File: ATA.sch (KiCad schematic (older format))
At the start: 12 parts, among them J1 TCOUPLE_IN, J2 Conn_01x08_Male, U1 AD8495, U2 AD8605

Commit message: updates
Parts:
- U2: symbol dk_Linear-Amplifiers-Instrumentation-OP-Amps-Buffer-Amps:AD8605ARTZ-REEL7 -> ATA-rescue:AD8605ARTZ-REEL7-dk_Linear-Amplifiers-Instrumentation-OP-Amps-Buffer-Amps
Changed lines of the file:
@@
 	5800 3400 5900 3400
 $Comp
-L dk_Linear-Amplifiers-Instrumentation-OP-Amps-Buffer-Amps:AD8605ARTZ-REEL7 U2
+L ATA-rescue:AD8605ARTZ-REEL7-dk_Linear-Amplifiers-Instrumentation-OP-Amps-Buffer-Amps U2
 U 1 1 5DF80621
 P 6700 4750

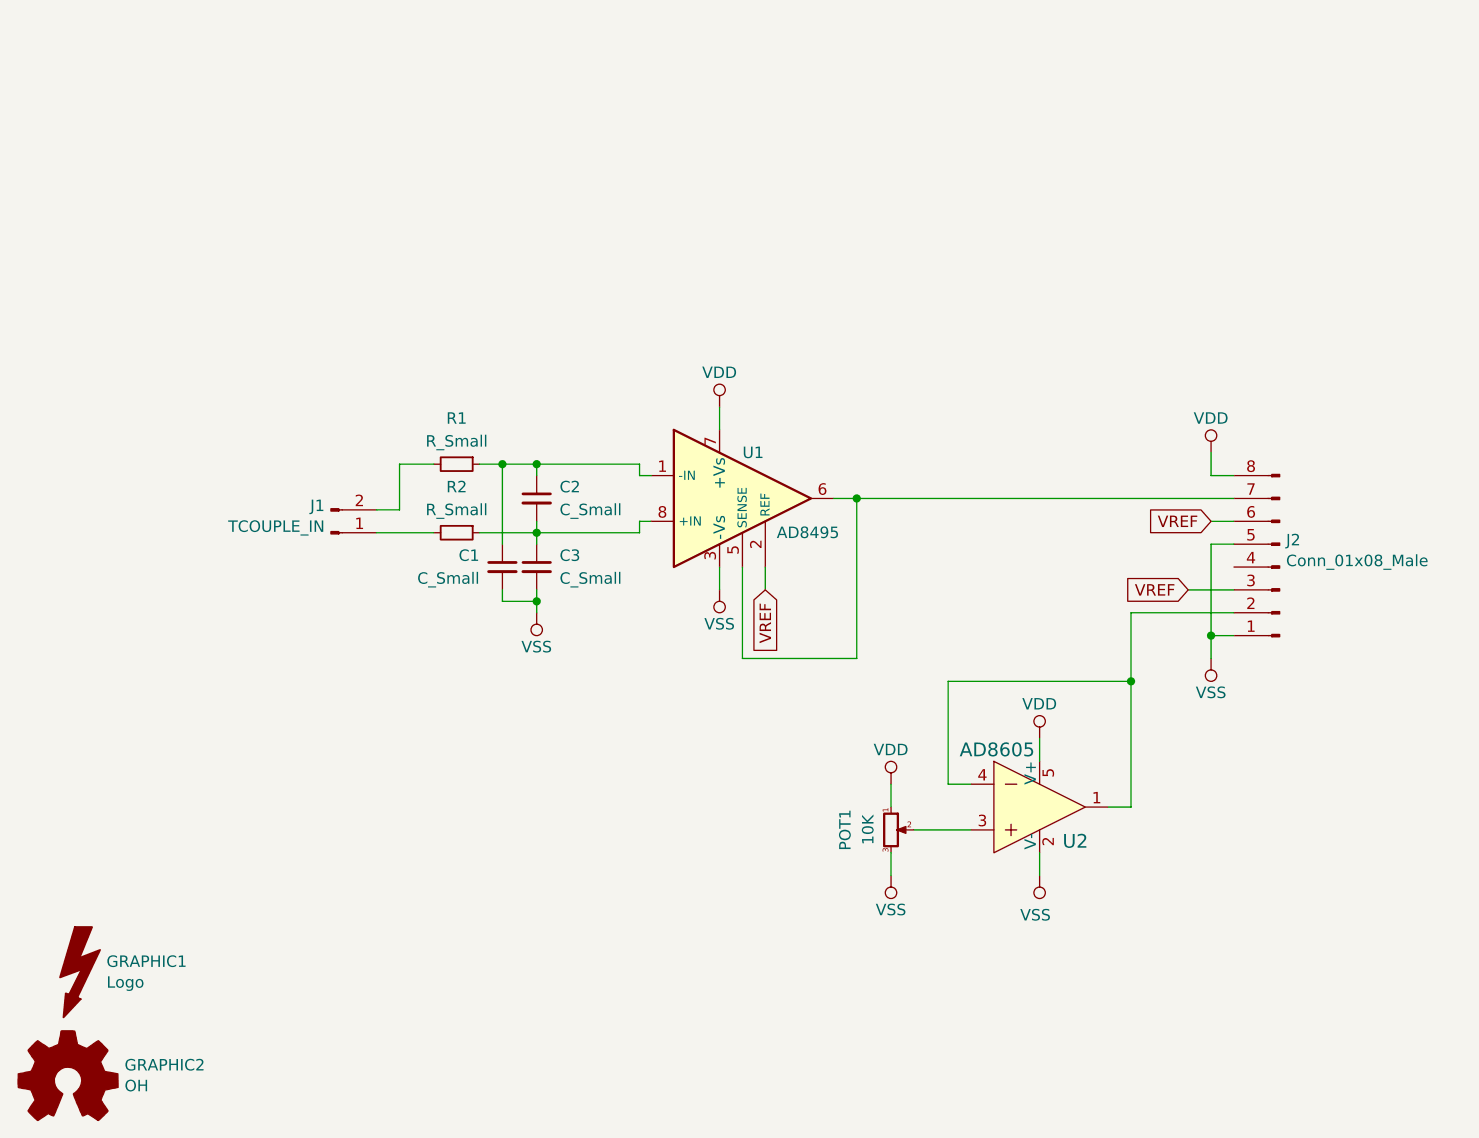
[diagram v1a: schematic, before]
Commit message: Added voltage reference chip to high side of adjustable voltage divider reference
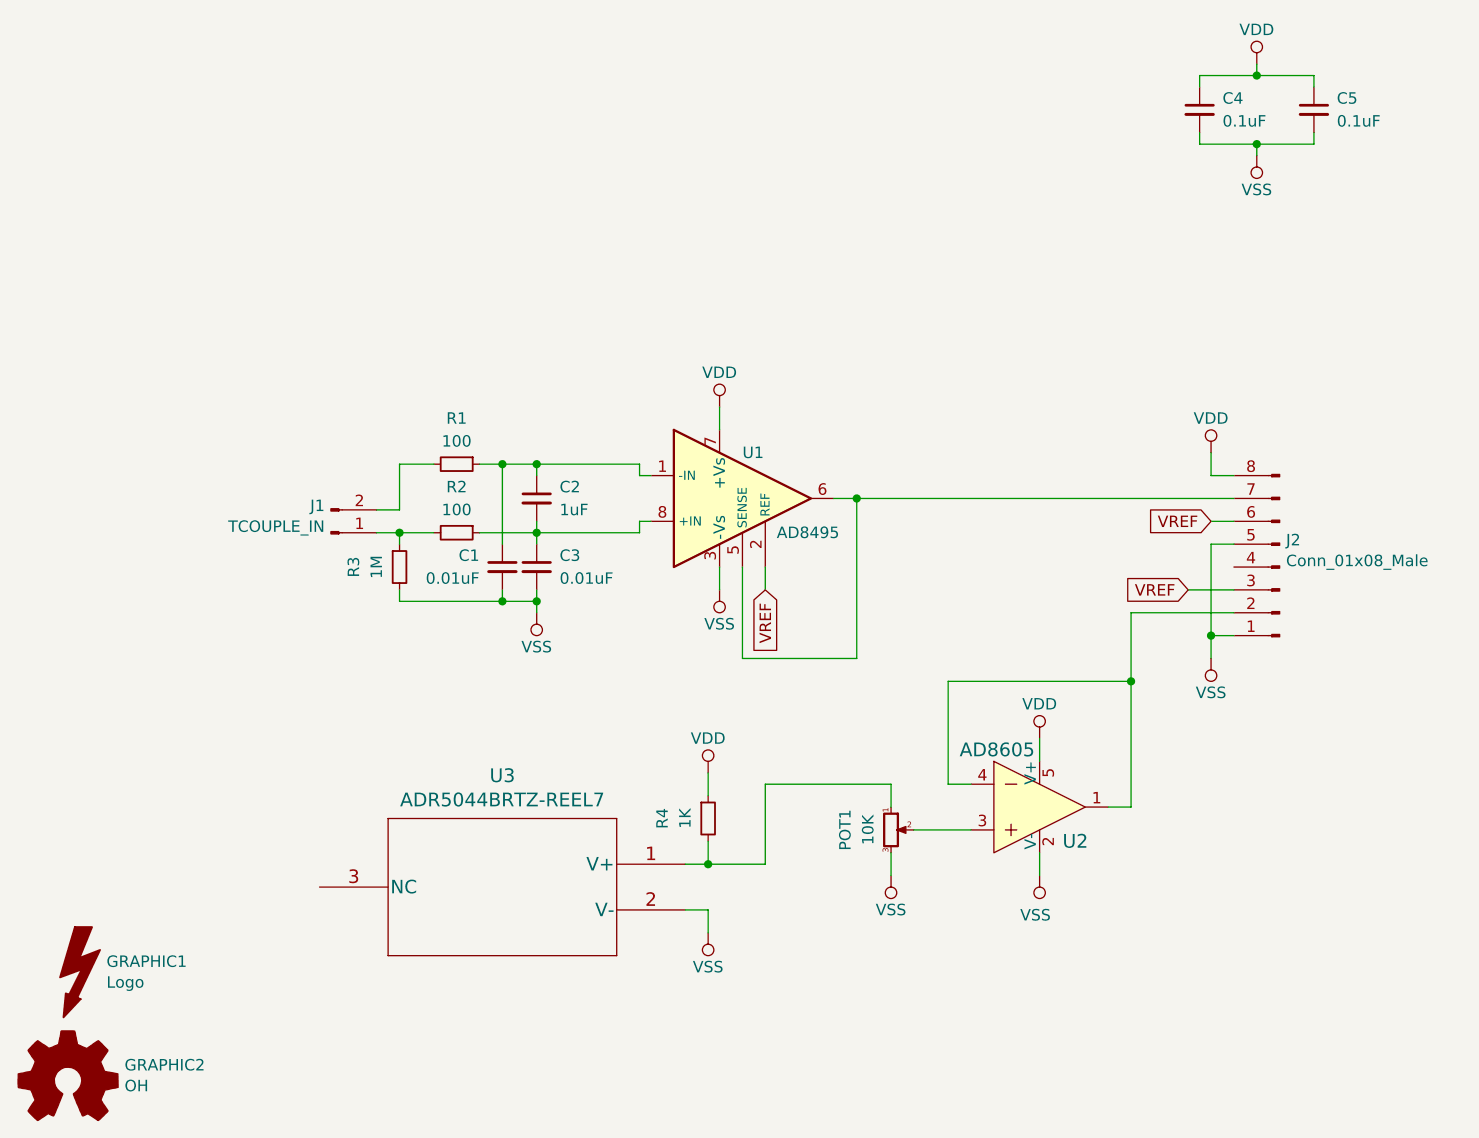
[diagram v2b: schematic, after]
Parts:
- added C4, C5: 0.1uF, Capacitor_SMD:C_0603_1608Metric, symbol Device:C_Small
- added R3: 1M, Resistor_SMD:R_0603_1608Metric, symbol Device:R_Small
- added R4: 1K, Resistor_SMD:R_0603_1608Metric, symbol Device:R_Small
- added U3: ADR5044BRTZ-REEL7, Package_TO_SOT_SMD:SOT-23, symbol ADR5044:ADR5044BRTZ-REEL7
- C1, C3: value C_Small -> 0.01uF
- C2: value C_Small -> 1uF
- R1, R2: value R_Small -> 100
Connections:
- net VDD: now also C4.1, C5.1, R4.1; no longer POT1.1
- net VSS: now also C4.2, C5.2, R3.2, U3.2 (V-)
- net at J1.1 (Pin_1), R2.2: now also R3.1
- new net: POT1.1, R4.2, U3.1 (V+)
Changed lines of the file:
@@
-$EndComp
-$Comp
-L power:VDD #PWR0101
-U 1 1 5DF499BB
-P 6050 4650
-F 0 "#PWR0101" H 6050 4500 50  0001 C CNN
-F 1 "VDD" H 6050 4800 50  0000 C CNN
-F 2 "" H 6050 4650 50  0001 C CNN
-F 3 "" H 6050 4650 50  0001 C CNN
-	1    6050 4650
-	1    0    0    -1
 $EndComp
 $Comp
@@
 P 4500 3400
 F 0 "C2" H 4600 3450 50  0000 L CNN
-F 1 "C_Small" H 4600 3350 50  0000 L CNN
+F 1 "1uF" H 4600 3350 50  0000 L CNN
 F 2 "Capacitor_SMD:C_0603_1608Metric" H 4500 3400 50  0001 C CNN
 F 3 "~" H 4500 3400 50  0001 C CNN
@@
 P 4500 3700
 F 0 "C3" H 4600 3750 50  0000 L CNN
-F 1 "C_Small" H 4600 3650 50  0000 L CNN
+F 1 "0.01uF" H 4600 3650 50  0000 L CNN
 F 2 "Capacitor_SMD:C_0603_1608Metric" H 4500 3700 50  0001 C CNN
 F 3 "~" H 4500 3700 50  0001 C CNN
@@
 P 4350 3700
 F 0 "C1" H 4250 3750 50  0000 R CNN
-F 1 "C_Small" H 4250 3650 50  0000 R CNN
+F 1 "0.01uF" H 4250 3650 50  0000 R CNN
 F 2 "Capacitor_SMD:C_0603_1608Metric" H 4350 3700 50  0001 C CNN
 F 3 "~" H 4350 3700 50  0001 C CNN
@@
 P 4150 3250
 F 0 "R1" V 3950 3250 50  0000 C CNN
-F 1 "R_Small" V 4050 3250 50  0000 C CNN
+F 1 "100" V 4050 3250 50  0000 C CNN
 F 2 "Resistor_SMD:R_0603_1608Metric" H 4150 3250 50  0001 C CNN
 F 3 "~" H 4150 3250 50  0001 C CNN
@@
 P 4150 3550
 F 0 "R2" V 3950 3550 50  0000 C CNN
-F 1 "R_Small" V 4050 3550 50  0000 C CNN
+F 1 "100" V 4050 3550 50  0000 C CNN
 F 2 "Resistor_SMD:R_0603_1608Metric" H 4150 3550 50  0001 C CNN
 F 3 "~" H 4150 3550 50  0001 C CNN
@@
 	4500 3850 4500 3800
 Wire Wire Line
-	3800 3550 4050 3550
+	3800 3550 3900 3550
 Wire Wire Line
 	3800 3450 3900 3450
@@
 	7550 3400 5900 3400
 Connection ~ 5900 3400
+$Comp
+L Device:R_Small R3
+U 1 1 5E27C7DB
+P 3900 3700
+F 0 "R3" V 3700 3700 50  0000 C CNN
+F 1 "1M" V 3800 3700 50  0000 C CNN
+F 2 "Resistor_SMD:R_0603_1608Metric" H 3900 3700 50  0001 C CNN
+F 3 "~" H 3900 3700 50  0001 C CNN
+	1    3900 3700
+	1    0    0    -1
+$EndComp
+Wire Wire Line
+	3900 3600 3900 3550
+Connection ~ 3900 3550
+Wire Wire Line
+	3900 3550 4050 3550
+Wire Wire Line
+	3900 3800 3900 3850
+Wire Wire Line
+	3900 3850 4350 3850
+Connection ~ 4350 3850
+$Comp
+L ADR5044:ADR5044BRTZ-REEL7 U3
+U 1 1 5E285920
+P 5150 5000
+F 0 "U3" H 5950 5387 60  0000 C CNN
+F 1 "ADR5044BRTZ-REEL7" H 5950 5281 60  0000 C CNN
+F 2 "Package_TO_SOT_SMD:SOT-23" H 5950 5240 60  0001 C CNN
+F 3 "" H 5150 5000 60  0000 C CNN
+	1    5150 5000
+	-1   0    0    -1
+$EndComp
+$Comp
+L power:VSS #PWR0101
+U 1 1 5E288407
+P 5250 5300
+F 0 "#PWR0101" H 5250 5150 50  0001 C CNN
+F 1 "VSS" H 5250 5450 50  0000 C CNN
+F 2 "" H 5250 5300 50  0001 C CNN
+F 3 "" H 5250 5300 50  0001 C CNN
+	1    5250 5300
+	-1   0    0    1
+$EndComp
+Wire Wire Line
+	5250 5300 5250 5200
+Wire Wire Line
+	5250 5200 5150 5200
+$Comp
+L power:VDD #PWR0103
+U 1 1 5E28A28E
+P 5250 4600
+F 0 "#PWR0103" H 5250 4450 50  0001 C CNN
+F 1 "VDD" H 5250 4750 50  0000 C CNN
+F 2 "" H 5250 4600 50  0001 C CNN
+F 3 "" H 5250 4600 50  0001 C CNN
+	1    5250 4600
+	1    0    0    -1
+$EndComp
+$Comp
+L Device:R_Small R4
+U 1 1 5E28BB5C
+P 5250 4800
+F 0 "R4" V 5050 4800 50  0000 C CNN
+F 1 "1K" V 5150 4800 50  0000 C CNN
+F 2 "Resistor_SMD:R_0603_1608Metric" H 5250 4800 50  0001 C CNN
+F 3 "~" H 5250 4800 50  0001 C CNN
+	1    5250 4800
+	1    0    0    -1
+$EndComp
+Wire Wire Line
+	5250 4700 5250 4600
+Wire Wire Line
+	5150 5000 5250 5000
+Wire Wire Line
+	5250 5000 5250 4900
+Wire Wire Line
+	5250 5000 5500 5000
+Wire Wire Line
+	5500 5000 5500 4650
+Wire Wire Line
+	5500 4650 6050 4650
+Connection ~ 5250 5000
+$Comp
+L Device:C_Small C4
+U 1 1 5E293563
+P 7400 1700
+F 0 "C4" H 7500 1750 50  0000 L CNN
+F 1 "0.1uF" H 7500 1650 50  0000 L CNN
+F 2 "Capacitor_SMD:C_0603_1608Metric" H 7400 1700 50  0001 C CNN
+F 3 "~" H 7400 1700 50  0001 C CNN
+	1    7400 1700
+	1    0    0    -1
+$EndComp
+$Comp
+L Device:C_Small C5
+U 1 1 5E29C4D5
+P 7900 1700
+F 0 "C5" H 8000 1750 50  0000 L CNN
+F 1 "0.1uF" H 8000 1650 50  0000 L CNN
+F 2 "Capacitor_SMD:C_0603_1608Metric" H 7900 1700 50  0001 C CNN
+F 3 "~" H 7900 1700 50  0001 C CNN
+	1    7900 1700
+	1    0    0    -1
+$EndComp
+$Comp
+L power:VSS #PWR0111
+U 1 1 5E29CBCA
+P 7650 1900
+F 0 "#PWR0111" H 7650 1750 50  0001 C CNN
+F 1 "VSS" H 7650 2050 50  0000 C CNN
+F 2 "" H 7650 1900 50  0001 C CNN
+F 3 "" H 7650 1900 50  0001 C CNN
+	1    7650 1900
+	-1   0    0    1
+$EndComp
+$Comp
+L power:VDD #PWR0112
+U 1 1 5E29E5BE
+P 7650 1500
+F 0 "#PWR0112" H 7650 1350 50  0001 C CNN
+F 1 "VDD" H 7650 1650 50  0000 C CNN
+F 2 "" H 7650 1500 50  0001 C CNN
+F 3 "" H 7650 1500 50  0001 C CNN
+	1    7650 1500
+	1    0    0    -1
+$EndComp
+Wire Wire Line
+	7400 1600 7400 1550
+Wire Wire Line
+	7400 1550 7650 1550
+Wire Wire Line
+	7650 1550 7650 1500
+Wire Wire Line
+	7650 1550 7900 1550
+Wire Wire Line
+	7900 1550 7900 1600
+Connection ~ 7650 1550
+Wire Wire Line
+	7400 1800 7400 1850
+Wire Wire Line
+	7400 1850 7650 1850
+Wire Wire Line
+	7650 1850 7650 1900
+Wire Wire Line
+	7650 1850 7900 1850
+Wire Wire Line
+	7900 1850 7900 1800
+Connection ~ 7650 1850
 $EndSCHEMATC

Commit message: Rearranged placement a bit. Generated CAM files for v2
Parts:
- U3: symbol ADR5044:ADR5044BRTZ-REEL7 -> ATA-rescue:ADR5044BRTZ-REEL7-ADR5044
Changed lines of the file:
@@
 Connection ~ 4350 3850
 $Comp
-L ADR5044:ADR5044BRTZ-REEL7 U3
+L ATA-rescue:ADR5044BRTZ-REEL7-ADR5044 U3
 U 1 1 5E285920
 P 5150 5000
